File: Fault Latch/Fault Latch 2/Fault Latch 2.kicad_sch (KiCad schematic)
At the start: 110 parts, among them K101 Fujitsu_FTR-LYAA005x, K102 Fujitsu_FTR-LYAA005x, K103 Fujitsu_FTR-LYAA005x, Q101 Q_NPN_BEC, Q102 Q_NPN_BEC, Q103 Q_NPN_BEC, Q104 Q_NPN_BEC, Q105 Q_NMOS_GSD, Q106 Q_NMOS_GSD, Q107 Q_PMOS_GSD, Q108 Q_PMOS_GSD, Q109 Q_PMOS_GSD, Q110 Q_NPN_BEC, Q111 Q_NPN_BEC, Q112 Q_NMOS_GSD, Q113 Q_PMOS_GSD, Q114 Q_NMOS_GSD, Q115 Q_NMOS_GSD, SW101 SW_Omron_B3FS, SW102 SW_Omron_B3FS, SW103 SW_Omron_B3FS, U101 SFH617A-1, U102 SFH617A-1, U103 SFH617A-1, U104 74AHC1G00, U105 74AHC1G00, U106 74AHC1G00, U107 74LS279, U108 641964-1, U109 SFH617A-1, U110 SFH617A-1, U111 641964-1, U112 641964-1, U113 641964-1, U114 641964-1, U115 641964-1, U116 641964-1, U117 74AHC1G00, U118 LM555xM, U119 74AHC1G00, U120 641964-1, U121 SFH617A-1, U122 641964-1, U123 641964-1

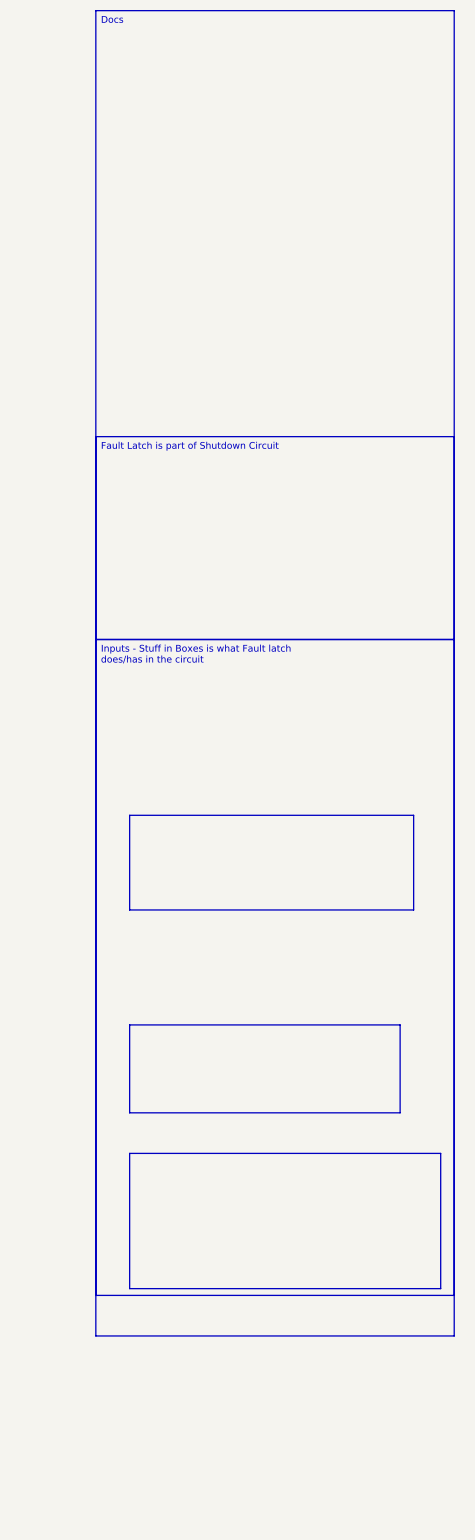
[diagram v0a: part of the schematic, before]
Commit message: Added more docs to Fault Latch
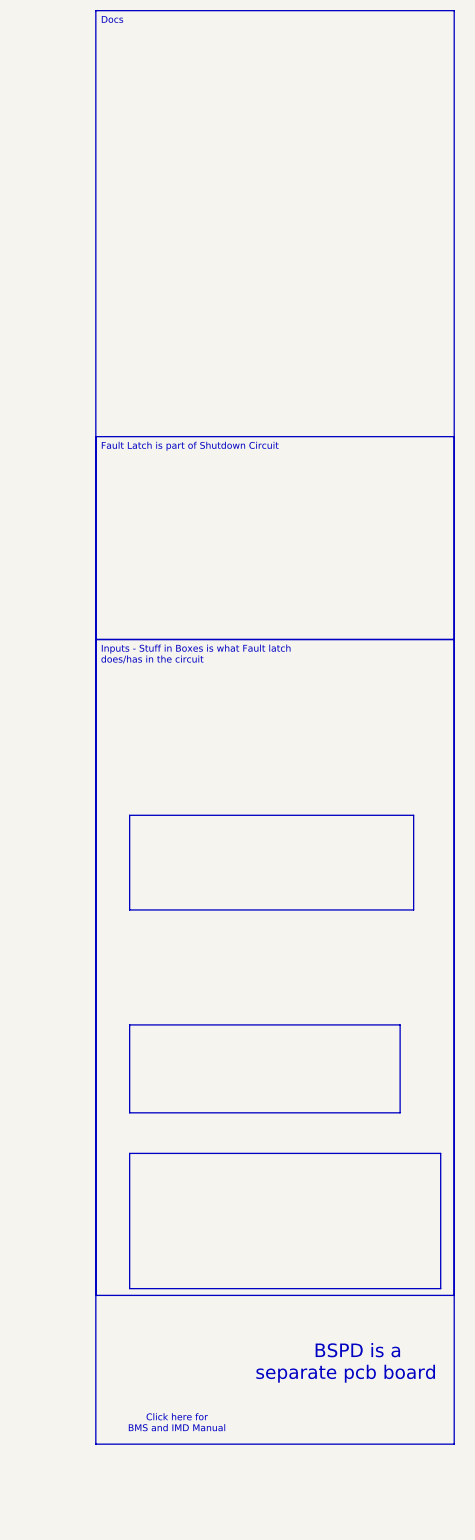
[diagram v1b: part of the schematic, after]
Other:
- note added: "BSPD is a separate pcb board"
- note added: "Click here for BMS and IMD Manual"

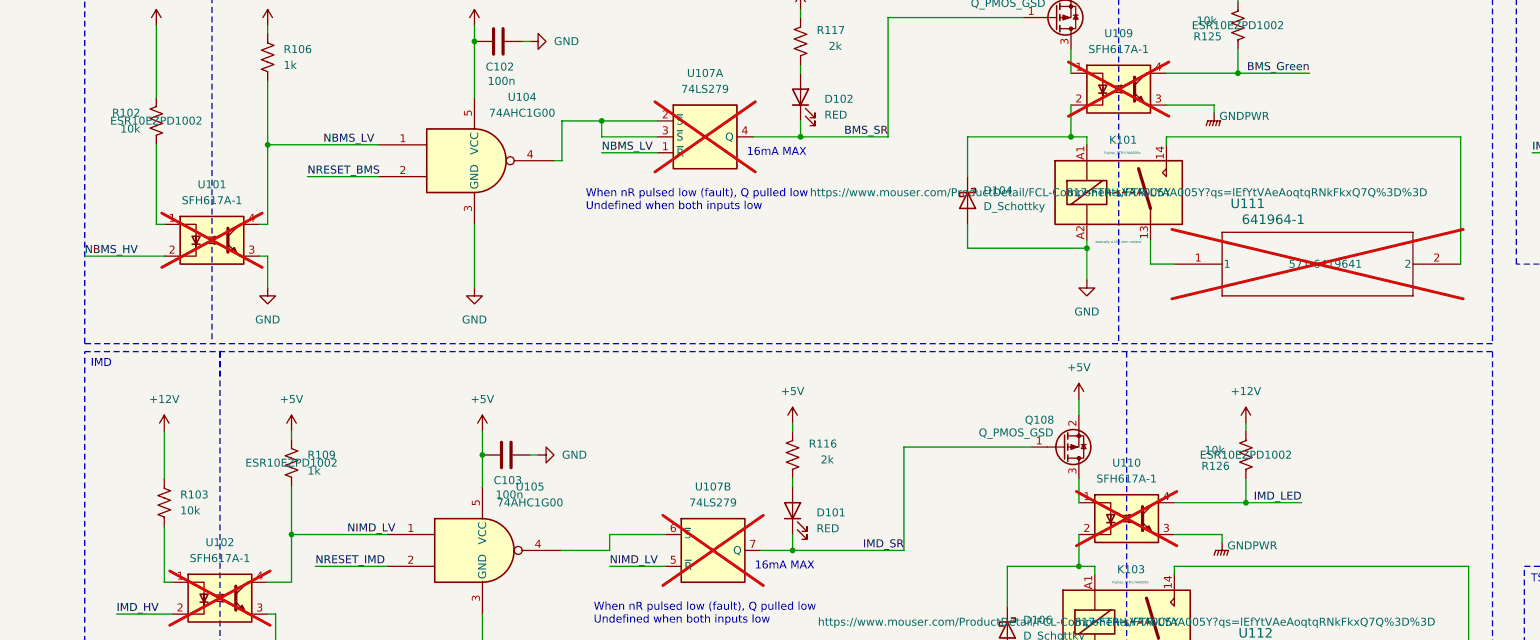
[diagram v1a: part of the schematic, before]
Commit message: RML through hole part 1
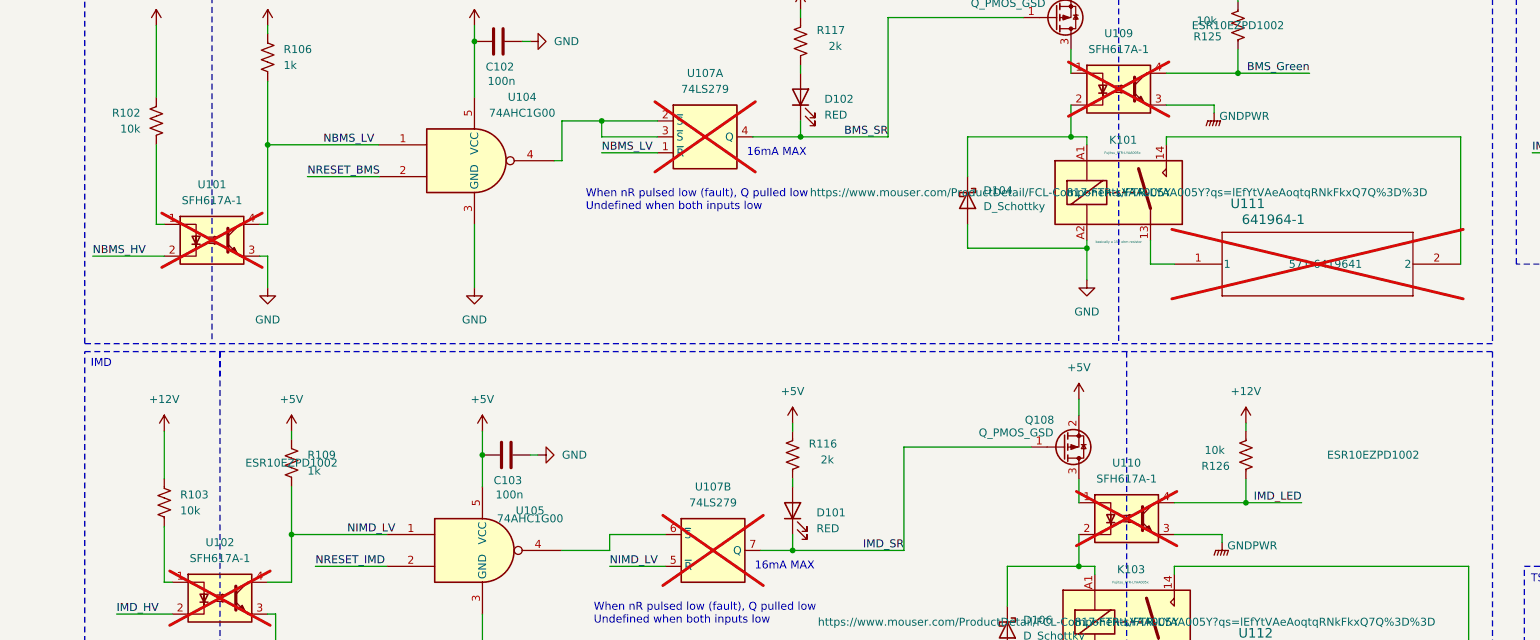
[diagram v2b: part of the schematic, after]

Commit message: Fixed Fault Latch optocoupler
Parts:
- R102, R103, R104: value 10k -> 100
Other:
- note added: "Click Here"

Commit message: Revised Fault Latch Layout
Fixed the schematic, did layout and wiring. Check for size and missed wires.
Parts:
- removed PS101: RI-1205S, DC-DC:RI0505S, symbol DC-DC:RI-1205S
- removed R1: R_US, symbol Device:R_US
- removed U108, U111, U112, U113, U114, U115, U116, U120, U123: 641964-1, 641964-1:TE_641964-1, symbol CONNECTOR:641964-1
- added J1: 1053141312, footprints:CONN_SD-105314-100_12_MOL, symbol 2025-10-04_18-31-19:1053141312
- added J2: 1053141106, molex.6-pin.footprint:CONN_SD-105314-100_06_MOL, symbol molex.6-pin:1053141106
- added J3: 1053131202, molex.2-pin.footprint:CONN_SD-105313-100_02_MOL, symbol molex.2-pin:1053131202
- added R137: 10k, Resistor_SMD:R_0805_2012Metric_Pad1.20x1.40mm_HandSolder, symbol Device:R_US
- added U1: LM1117DTX-5.0_NOPB, LM1117DTX-5.0_NOPB:TO228P970X238-3N, symbol LM1117DTX-5.0_NOPB:LM1117DTX-5.0_NOPB
- R102: value 100 -> 220; footprint Resistor_SMD:R_0805_2012Metric_Pad1.20x1.40mm_HandSolder -> Resistor_SMD:R_0201_0603Metric; JLC# (none) -> C384419
- R103: value 100 -> 220; footprint Resistor_SMD:R_0805_2012Metric_Pad1.20x1.40mm_HandSolder -> Resistor_SMD:R_0201_0603Metric; JLC# C17520 -> C384419
- R104: value 100 -> 220; JLC# C17414 -> C384419
- R121, R136: JLC# (none) -> C17414
- R133: value 10k -> 220; JLC# C105637 -> C384419
- R134: JLC# C105637 -> (none)
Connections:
- net BMS_GREEN is gone; now on net BMS_Green: Q114.1 (G)
- net GNDPWR is gone; now on net GND: C113.2, C114.2, C115.2, Q105.2 (S), Q106.2 (S), Q112.2 (S), Q114.2 (S), Q115.2 (S), U109.3, U110.3, U121.3, U122.1
- net +12V: now also J3.1, R137.1, U1.3 (VIN)
- net +5V: now also U1.2 (VOUT)
- net GND: now also J3.2, U1.1 (ADJ_/_GND)
- net IMD Out: now reaches K103.13
- net IMD Out: now also J2.4
- net IMD In: now reaches K103.14
- net IMD In: now also J2.3
- net IMD Light Out: now reaches Q106.3 (D)
- net IMD Light Out: now also J1.7
- net IMD Light In: now reaches R112.2
- net IMD Light In: now also J1.6
- net BMS Out: now reaches K101.13
- net BMS Out: now also J2.2
- net Shutdown Circuit In: now reaches K101.14
- net Shutdown Circuit In: now also J2.1
- net TSSI Green Out: now reaches Q112.3 (D)
- net TSSI Green Out: now also J1.9
- net TSSI Green In: now reaches R130.1
- net TSSI Green In: now also J1.8
- net BMS Light Out: now reaches Q115.3 (D)
- net BMS Light Out: now also J1.5
- net Shutdown Circuit Out: now reaches K102.13
- net Shutdown Circuit Out: now also J2.6
- net at D1.2 (A), D2.2 (A), Q112.1 (G): now also R137.2
- net BMS Light In: now reaches R135.2
- net BMS Light In: now also J1.4
- new net BPSD HV: J1.3
- new net BPSD In: J2.5
- new net IMD HV: J1.2
- new net NBMS HV: J1.1
- new net TSSI Red In: J1.10
- new net TSSI Red Out: J1.11
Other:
- moved on the sheet: C107, C108, C113, C114, C115, C116, C117, H101, H102, H103, H104, U107E

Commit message: Fault Latch Layout revised
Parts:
- removed U1: LM1117DTX-5.0_NOPB, LM1117DTX-5.0_NOPB:TO228P970X238-3N, symbol LM1117DTX-5.0_NOPB:LM1117DTX-5.0_NOPB
- removed U122: 641964-1, 641964-1:TE_641964-1, symbol CONNECTOR:641964-1
- added Q116: Q_NMOS_GSD, Package_TO_SOT_SMD:SOT-23, symbol Transistor_FET:Q_NMOS_GSD
- added R138: 10k, Resistor_SMD:R_0805_2012Metric_Pad1.20x1.40mm_HandSolder, symbol Device:R_US
- added U2: LM1117DT-5.0, Package_TO_SOT_SMD:TO-252-3_TabPin2, symbol Regulator_Linear:LM1117DT-5.0
- R104: footprint Resistor_SMD:R_0805_2012Metric_Pad1.20x1.40mm_HandSolder -> Resistor_SMD:R_0201_0603Metric
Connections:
- net TSSI Red Out is gone; now on net IMD HV: J1.11
- net +12V: now also J3.2, R138.1, U2.3 (VI); no longer J3.1
- net +5V: now also U2.2 (VO)
- net BMS Light In: now also J1.9; no longer J1.4
- net BMS Light Out: now also J1.2; no longer J1.5
- net BPSD HV: now also J1.10; no longer J1.3
- net BPSD In: now also K102.14
- net GND: now also J1.1, J3.1, Q116.2 (S), U2.1 (GND); no longer J3.2
- net IMD HV: no longer J1.2
- net IMD Light Out: now also J1.5; no longer J1.7
- net NBMS HV: now also J1.12; no longer J1.1
- net TSSI Green In: now also J1.4; no longer J1.8
- net TSSI Green Out: now also J1.3; no longer J1.9
- net TSSI Red In: now also J1.8, Q113.3 (D); no longer J1.10
- net at D1.2 (A), D2.2 (A), R137.2: now also Q116.1 (G); no longer Q112.1 (G)
- new net: Q112.1 (G), Q116.3 (D), R138.2
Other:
- moved on the sheet: C113, C114, C115, C116, D1, D2, J3, Q112, Q113, R130, R134, R137

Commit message: Fault Latch Updates
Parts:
- removed J2: 1053141106, molex.6-pin.footprint:CONN_SD-105314-100_06_MOL, symbol molex.6-pin:1053141106
- added J4: 1053131202, Connector_Molex:Molex_Nano-Fit_105313-xx02_1x02_P2.50mm_Horizontal, symbol molex.2-pin:1053131202
- J3: footprint molex.2-pin.footprint:CONN_SD-105313-100_02_MOL -> Connector_Molex:Molex_Nano-Fit_105313-xx02_1x02_P2.50mm_Horizontal
- R102: footprint Resistor_SMD:R_0201_0603Metric -> Resistor_SMD:R_0805_2012Metric_Pad1.20x1.40mm_HandSolder; JLC# C384419 -> C2074007; MOUSER ESR10EZPD1002 -> (none)
- R103, R104: footprint Resistor_SMD:R_0201_0603Metric -> Resistor_SMD:R_0805_2012Metric_Pad1.20x1.40mm_HandSolder; JLC# C384419 -> C2074007
- R133: footprint Resistor_SMD:R_0603_1608Metric -> Resistor_SMD:R_0805_2012Metric_Pad1.20x1.40mm_HandSolder; JLC# C384419 -> C2074007
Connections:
- net BPSD HV is gone; now on net BSPD_HV: J1.10
- net IMD HV is gone; now on net IMD_HV: J1.11
- net IMD In is gone; now on an unnamed net: K103.14
- net IMD Out is gone; now on an unnamed net: K103.13
- net NBMS HV is gone; now on net NBMS_HV: J1.12
- net BMS Light In: now also J1.2; no longer J1.9
- net BMS Light Out: now also J1.1; no longer J1.2
- net GND: now also J1.7; no longer J1.1
- net Shutdown Circuit In: now also J4.1
- net Shutdown Circuit Out: now also J4.2
- net BMS Out: no longer names the net of K101.13
- net BPSD In: no longer names the net of K102.14
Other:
- moved on the sheet: J3

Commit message: Fault Latch Layout Pre-Bom 2025 check
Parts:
- removed D1, D2: SS12, Diode_SMD:D_SMA, symbol Diode:SS12
- added D107, D108: D_Schottky, Diode_SMD:D_SMA, symbol Device:D_Schottky
- J1: MOUSER (none) -> 538-105314-1312
- J3, J4: MOUSER (none) -> 538-105313-1202
- R105, R114, R123: MOUSER (none) -> ESR10EZPD1002
- R107, R109: MOUSER ESR10EZPD1002 -> (none)
- R112, R135: JLC# (none) -> KTR03EZPF5100
- R125, R126: JLC# (none) -> C17414
- R134: footprint Resistor_SMD:R_0603_1608Metric -> Resistor_SMD:R_0805_2012Metric_Pad1.20x1.40mm_HandSolder; JLC# (none) -> C17414; MOUSER (none) -> ESR10EZPD1002
- U2: JLC# (none) -> C354068
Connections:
- net BMS_Green: now also D108.1 (K)
- net IMD_LED: now also D107.1 (K)
- net at Q116.1 (G), R137.2: now also D107.2 (A), D108.2 (A)
